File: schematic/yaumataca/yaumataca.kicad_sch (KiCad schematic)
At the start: 33 parts, among them J1 Joystick Port, J2 Mouse Port, J3 Conn_02x05_Odd_Even, J4 Conn_02x05_Odd_Even, Q1 BC547, Q10 BC547, Q11 BC547, Q12 BC547, Q13 BC547, Q14 BC547, Q2 BC547, Q3 BC547, Q4 BC547, Q5 BC547, Q6 BC547, Q7 BC547, Q8 BC547, Q9 BC547, U1 Pico

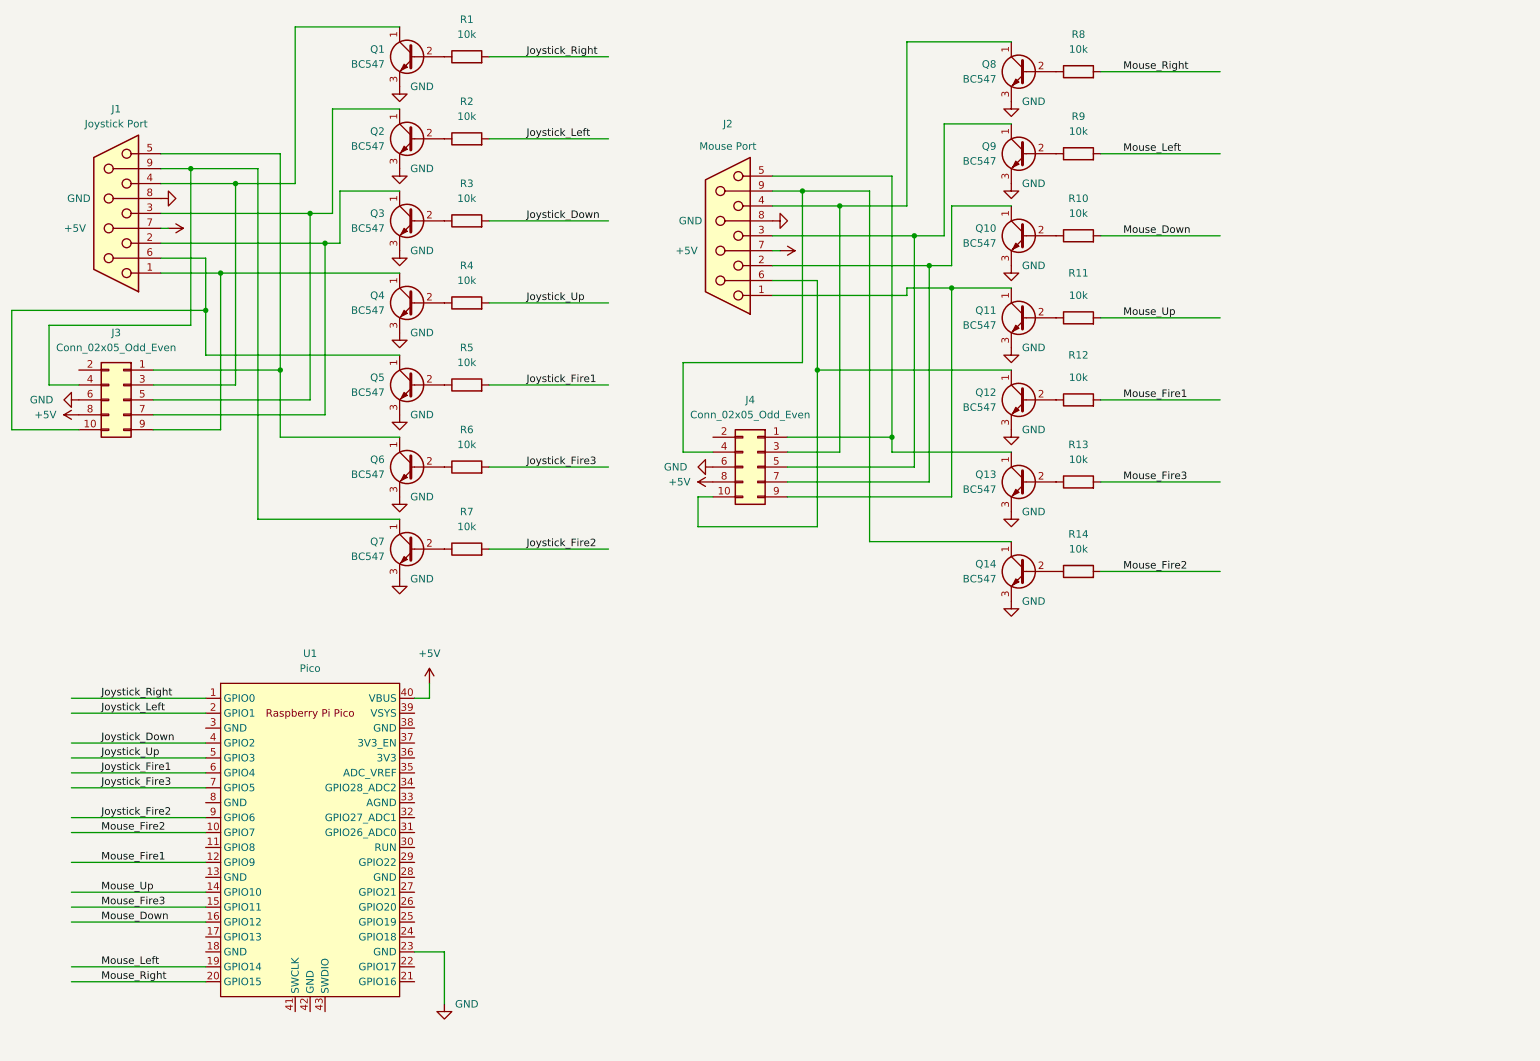
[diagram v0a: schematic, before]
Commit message: Documentation
Just a little bit more text.
Also updated schematics and created
some diagrams.
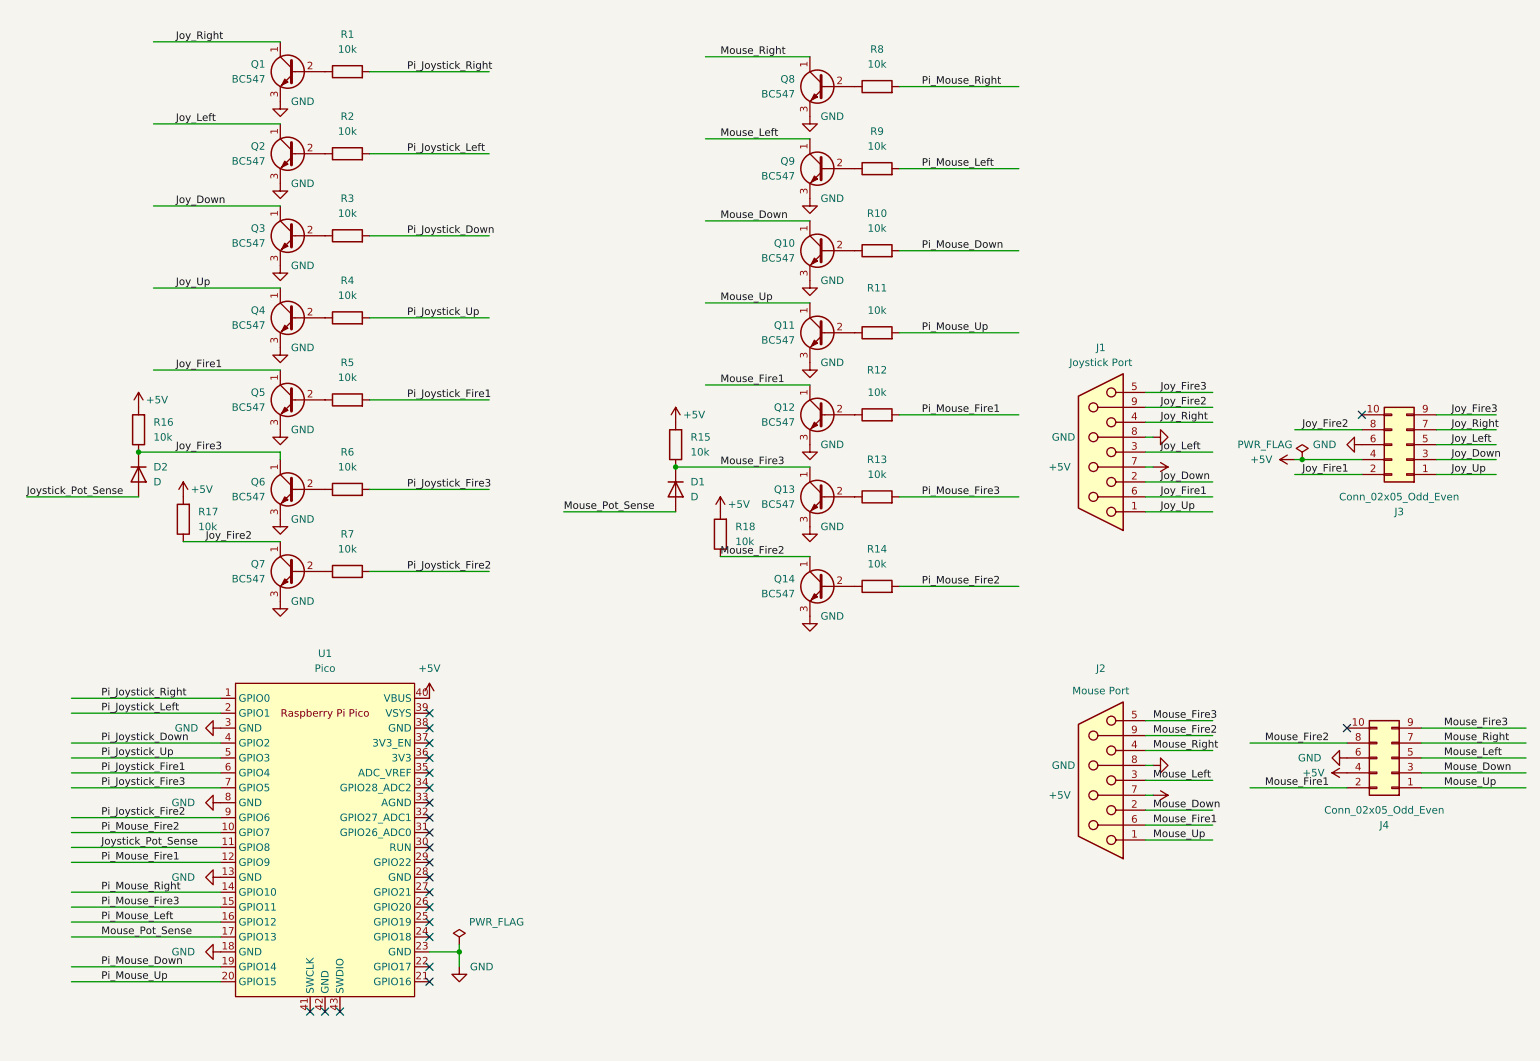
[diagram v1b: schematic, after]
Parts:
- added D1, D2: D, Diode_THT:D_T-1_P5.08mm_Horizontal, symbol Device:D
- added R15, R16, R17, R18: 10k, Resistor_THT:R_Axial_DIN0204_L3.6mm_D1.6mm_P7.62mm_Horizontal, symbol Device:R
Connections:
- net +5V: now also J3.4 (Pin_4), J4.4 (Pin_4), R15.2, R16.2, R17.2, R18.2; no longer J3.8 (Pin_8), J4.8 (Pin_8)
- net GND: now also U1.13 (GND), U1.18 (GND), U1.3 (GND), U1.8 (GND)
- net Mouse_Down: now also J2.2, J4.3 (Pin_3), Q10.1 (C); no longer R10.2, U1.16 (GPIO12)
- net Mouse_Fire1: now also J2.6, J4.2 (Pin_2), Q12.1 (C); no longer R12.2, U1.12 (GPIO9)
- net Mouse_Fire2: now also J2.9, J4.8 (Pin_8), Q14.1 (C), R18.1; no longer R14.2, U1.10 (GPIO7)
- net Mouse_Fire3: now also J2.5, J4.9 (Pin_9), Q13.1 (C), D1.1 (K), R15.1; no longer R13.2, U1.15 (GPIO11)
- net Mouse_Left: now also J2.3, J4.5 (Pin_5), Q9.1 (C); no longer R9.2, U1.19 (GPIO14)
- net Mouse_Right: now also J2.4, J4.7 (Pin_7), Q8.1 (C); no longer R8.2, U1.20 (GPIO15)
- net Mouse_Up: now also J2.1, J4.1 (Pin_1), Q11.1 (C); no longer R11.2, U1.14 (GPIO10)
- net Joy_Up: now reaches J1.1, Q4.1 (C)
- net Joy_Up: now also J3.1 (Pin_1); no longer J3.9 (Pin_9)
- net Joy_Down: now reaches J1.2, Q3.1 (C)
- net Joy_Down: now also J3.3 (Pin_3); no longer J3.7 (Pin_7)
- net Joy_Left: now reaches J1.3, J3.5 (Pin_5), Q2.1 (C)
- net Joy_Right: now reaches J1.4, Q1.1 (C)
- net Joy_Right: now also J3.7 (Pin_7); no longer J3.3 (Pin_3)
- net Joy_Fire3: now reaches J1.5, Q6.1 (C)
- net Joy_Fire3: now also J3.9 (Pin_9), D2.1 (K), R16.1; no longer J3.1 (Pin_1)
- net Joy_Fire1: now reaches J1.6, Q5.1 (C)
- net Joy_Fire1: now also J3.2 (Pin_2); no longer J3.10 (Pin_10)
- net Joy_Fire2: now reaches J1.9, Q7.1 (C)
- net Joy_Fire2: now also J3.8 (Pin_8), R17.1; no longer J3.4 (Pin_4)
- net Joystick_Pot_Sense: now reaches U1.11 (GPIO8)
- net Joystick_Pot_Sense: now also D2.2 (A)
- net Mouse_Pot_Sense: now reaches U1.17 (GPIO13)
- net Mouse_Pot_Sense: now also D1.2 (A)
- net Joystick_Down renamed Pi_Joystick_Down
- net Joystick_Fire1 renamed Pi_Joystick_Fire1
- net Joystick_Fire2 renamed Pi_Joystick_Fire2
- net Joystick_Fire3 renamed Pi_Joystick_Fire3
- net Joystick_Left renamed Pi_Joystick_Left
- net Joystick_Right renamed Pi_Joystick_Right
- net Joystick_Up renamed Pi_Joystick_Up
- new net Pi_Mouse_Down: R10.2, U1.19 (GPIO14)
- new net Pi_Mouse_Fire1: R12.2, U1.12 (GPIO9)
- new net Pi_Mouse_Fire2: R14.2, U1.10 (GPIO7)
- new net Pi_Mouse_Fire3: R13.2, U1.15 (GPIO11)
- new net Pi_Mouse_Left: R9.2, U1.16 (GPIO12)
- new net Pi_Mouse_Right: R8.2, U1.14 (GPIO10)
- new net Pi_Mouse_Up: R11.2, U1.20 (GPIO15)
- now unconnected: J4.10 (Pin_10)
- no-connect marks 0 -> 23
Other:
- moved on the sheet: J1, J2, J3, J4, Q1, Q10, Q11, Q12, Q13, Q14, Q2, Q3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

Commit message: First idea of a PCB
All components on one side
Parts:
- removed Q1, Q10, Q11, Q12, Q13, Q14, Q2, Q3, Q4, Q5, Q6, Q7, Q8, Q9: BC547, Package_TO_SOT_THT:TO-92_Inline_Wide, symbol Transistor_BJT:BC547
- removed R1, R10, R11, R12, R13, R14, R2, R3, R4, R5, R6, R7, R8, R9: 10k, Resistor_THT:R_Axial_DIN0204_L3.6mm_D1.6mm_P7.62mm_Horizontal, symbol Device:R
- added C1: C_Polarized, Capacitor_THT:CP_Radial_D10.0mm_P5.00mm, symbol Device:C_Polarized
- added L1: L_Ferrite, Inductor_THT:L_Axial_L5.3mm_D2.2mm_P7.62mm_Horizontal_Vishay_IM-1, symbol Device:L_Ferrite
- added Q1, Q10, Q11, Q12, Q13, Q14, Q2, Q3, Q4, Q5, Q6, Q7, Q8, Q9: DTC143Z, Package_TO_SOT_SMD:SOT-23_Handsoldering, symbol Transistor_BJT:DTC143Z
- D1, D2: footprint Diode_THT:D_T-1_P5.08mm_Horizontal -> Diode_SMD:D_1206_3216Metric_Pad1.42x1.75mm_HandSolder
- R15, R16, R17, R18: footprint Resistor_THT:R_Axial_DIN0204_L3.6mm_D1.6mm_P7.62mm_Horizontal -> Resistor_SMD:R_1206_3216Metric_Pad1.30x1.75mm_HandSolder
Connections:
- net +5V: now also L1.2; no longer U1.40 (VBUS)
- net GND: now also U1.42 (GND), C1.2, Q1.2 (E), Q10.2 (E), Q11.2 (E), Q12.2 (E), Q13.2 (E), Q14.2 (E), Q2.2 (E), Q3.2 (E), Q4.2 (E), Q5.2 (E), Q6.2 (E), Q7.2 (E), Q8.2 (E), Q9.2 (E)
- net Joy_Down: now also Q3.3 (C)
- net Joy_Fire1: now also Q5.3 (C)
- net Joy_Fire2: now also Q7.3 (C)
- net Joy_Fire3: now also Q6.3 (C)
- net Joy_Left: now also Q2.3 (C)
- net Joy_Right: now also Q1.3 (C)
- net Joy_Up: now also Q4.3 (C)
- net Mouse_Down: now also Q12.3 (C)
- net Mouse_Fire1: now also Q10.3 (C)
- net Mouse_Fire2: now also Q8.3 (C)
- net Mouse_Fire3: now also Q9.3 (C)
- net Mouse_Left: now also Q13.3 (C)
- net Mouse_Right: now also Q14.3 (C)
- net Mouse_Up: now also Q11.3 (C)
- net Pi_Joystick_Down: now also Q3.1 (B)
- net Pi_Joystick_Fire1: now also Q5.1 (B)
- net Pi_Joystick_Fire2: now also Q7.1 (B)
- net Pi_Joystick_Fire3: now also Q6.1 (B)
- net Pi_Joystick_Left: now also Q2.1 (B)
- net Pi_Joystick_Right: now also Q1.1 (B)
- net Pi_Joystick_Up: now also Q4.1 (B)
- net Pi_Mouse_Down: now also Q12.1 (B)
- net Pi_Mouse_Fire1: now also Q10.1 (B)
- net Pi_Mouse_Fire2: now also Q8.1 (B)
- net Pi_Mouse_Fire3: now also Q9.1 (B)
- net Pi_Mouse_Left: now also Q13.1 (B)
- net Pi_Mouse_Right: now also Q14.1 (B)
- net Pi_Mouse_Up: now also Q11.1 (B)
- new net: C1.1, L1.1, U1.40 (VBUS)

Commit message: Added ordered PCB
Components on both sides for an
even smaller size.
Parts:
- C1: value C_Polarized -> 1000u
- D1, D2: footprint Diode_SMD:D_1206_3216Metric_Pad1.42x1.75mm_HandSolder -> Diode_SMD:D_SOD-123
- J3, J4: footprint Connector_PinSocket_2.54mm:PinSocket_2x05_P2.54mm_Vertical -> Connector_IDC:IDC-Header_2x05_P2.54mm_Vertical
- L1: value L_Ferrite -> 100u
- Q1, Q10, Q11, Q12, Q13, Q14, Q2, Q3, Q4, Q5, Q6, Q7, Q8, Q9: footprint Package_TO_SOT_SMD:SOT-23_Handsoldering -> Library:SOT-23_ohnesilk
- R15, R16, R17, R18: footprint Resistor_SMD:R_1206_3216Metric_Pad1.30x1.75mm_HandSolder -> Resistor_SMD:R_0805_2012Metric_Pad1.20x1.40mm_HandSolder
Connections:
- net +5V: now also C1.1, L1.1, U1.40 (VBUS); no longer J3.4 (Pin_4), J4.4 (Pin_4), L1.2
- new net HOST_5V: J3.4 (Pin_4), J4.4 (Pin_4), L1.2
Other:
- moved on the sheet: J2
